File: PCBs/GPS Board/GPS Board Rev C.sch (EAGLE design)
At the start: 4 parts

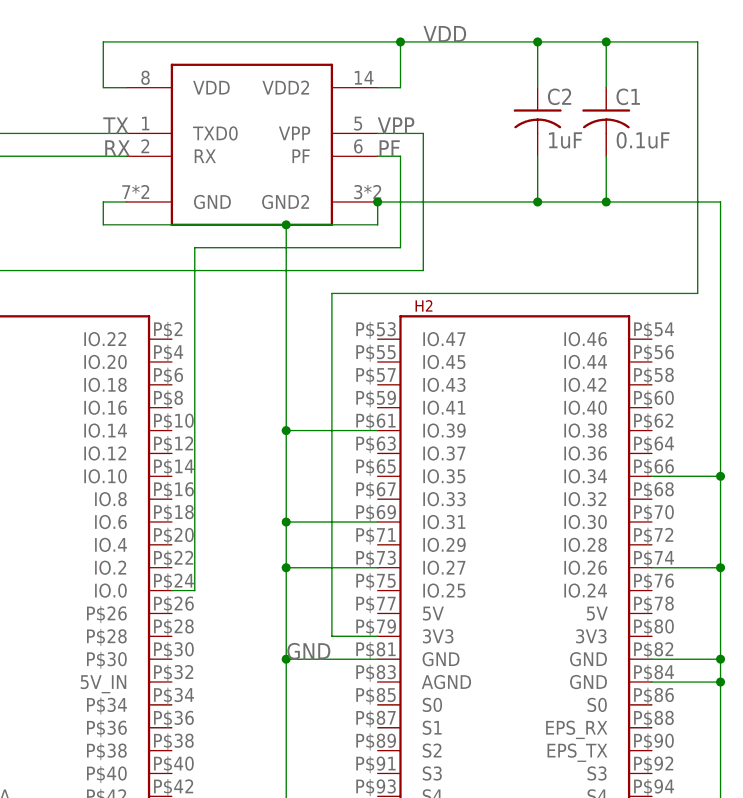
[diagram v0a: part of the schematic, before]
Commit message: Changed GPS power source to an EPS PDM, tweaked trace width
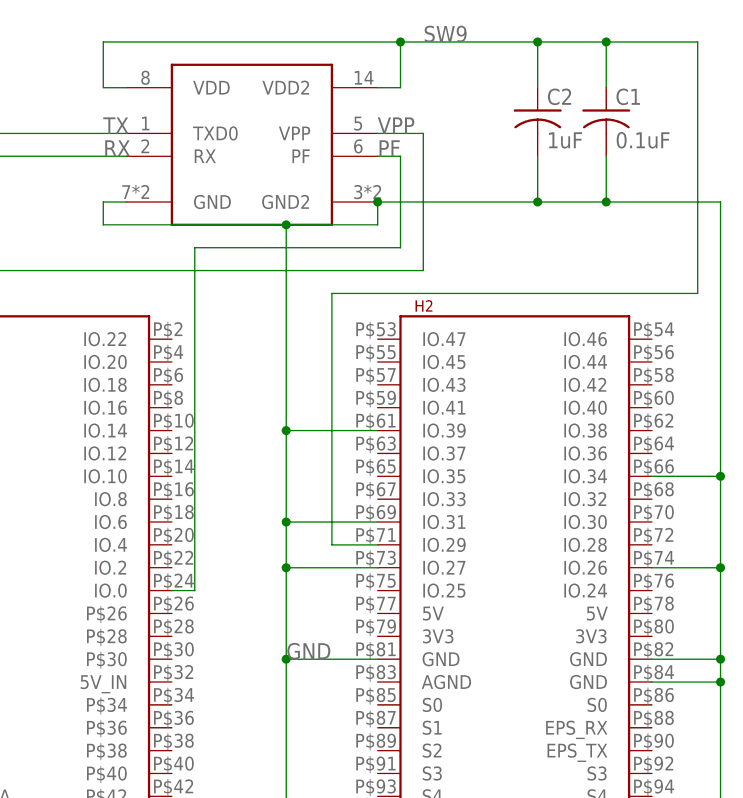
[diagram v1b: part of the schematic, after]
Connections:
- removed net VDD: C1.1, C2.1, U$1.VDD, U$1.VDD2, U$2.3V3@1
- new net SW9: C1.1, C2.1, U$1.VDD, U$1.VDD2, U$2.IO.29
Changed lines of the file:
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@@
 </busses>
 <nets>
-<net name="VDD" class="0">
+<net name="SW9" class="0">
 <segment>
 <wire x1="48.26" y1="91.44" x2="48.26" y2="86.36" width="0.1524" layer="91"/>
@@
 <wire x1="71.12" y1="91.44" x2="81.28" y2="91.44" width="0.1524" layer="91"/>
 <wire x1="81.28" y1="91.44" x2="81.28" y2="63.5" width="0.1524" layer="91"/>
-<wire x1="81.28" y1="63.5" x2="40.64" y2="63.5" width="0.1524" layer="91"/>
-<wire x1="40.64" y1="63.5" x2="40.64" y2="25.4" width="0.1524" layer="91"/>
-<pinref part="U$2" gate="G$1" pin="3V3@1"/>
-<wire x1="40.64" y1="25.4" x2="45.72" y2="25.4" width="0.1524" layer="91"/>
 <pinref part="C2" gate="G$1" pin="1"/>
 <wire x1="63.5" y1="86.36" x2="63.5" y2="91.44" width="0.1524" layer="91"/>
@@
 <pinref part="U$1" gate="G$1" pin="VDD"/>
 <wire x1="15.24" y1="86.36" x2="17.78" y2="86.36" width="0.1524" layer="91"/>
+<wire x1="81.28" y1="63.5" x2="40.64" y2="63.5" width="0.1524" layer="91"/>
+<pinref part="U$2" gate="G$1" pin="IO.29"/>
+<wire x1="40.64" y1="63.5" x2="40.64" y2="35.56" width="0.1524" layer="91"/>
+<wire x1="40.64" y1="35.56" x2="45.72" y2="35.56" width="0.1524" layer="91"/>
 </segment>
 </net>

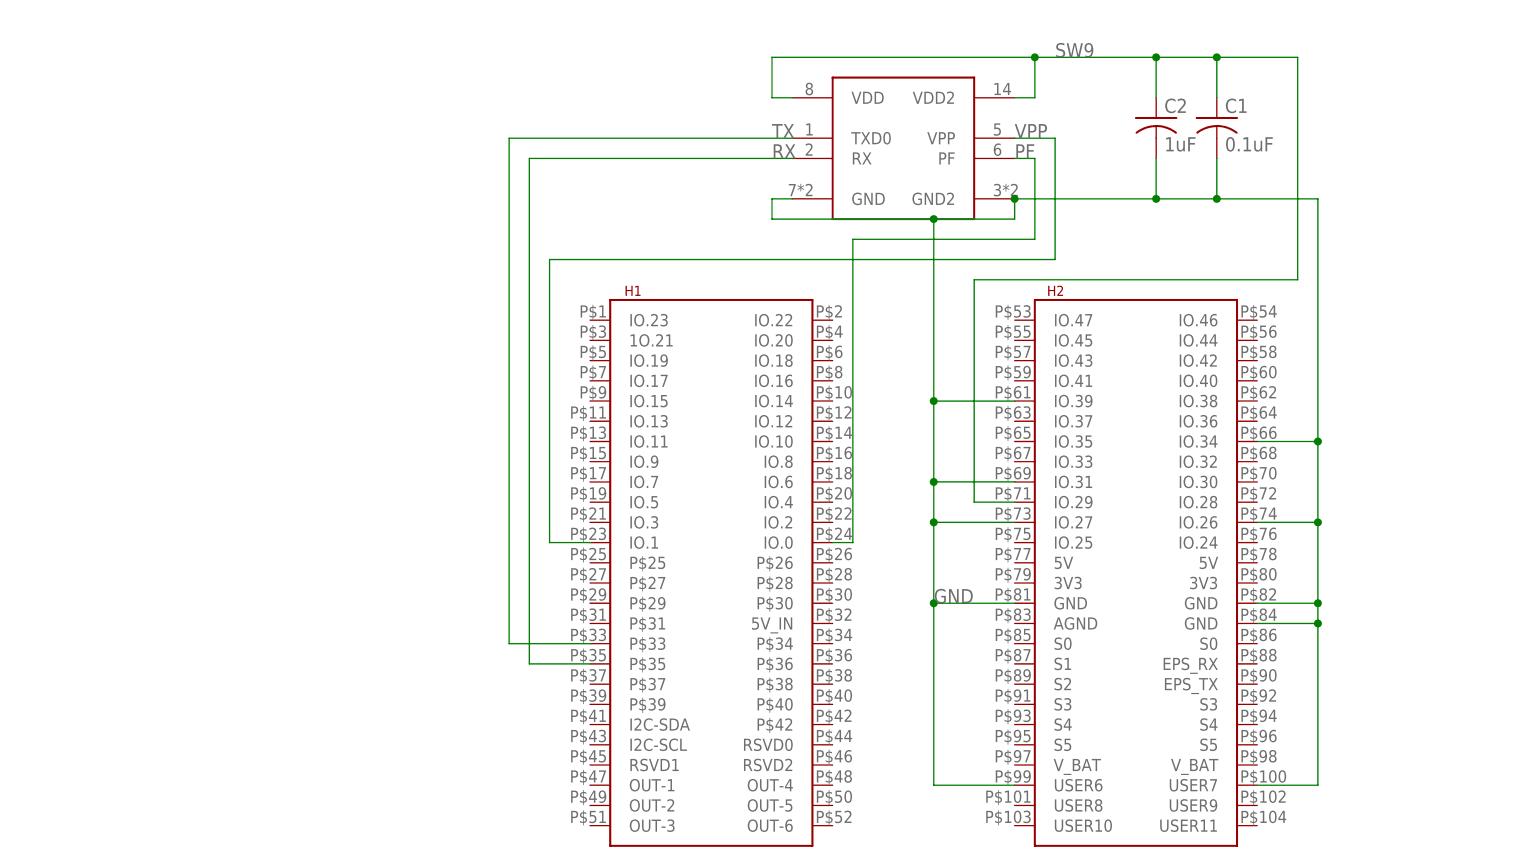
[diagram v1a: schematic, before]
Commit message: Add temp sensors to GPS and Radio boards
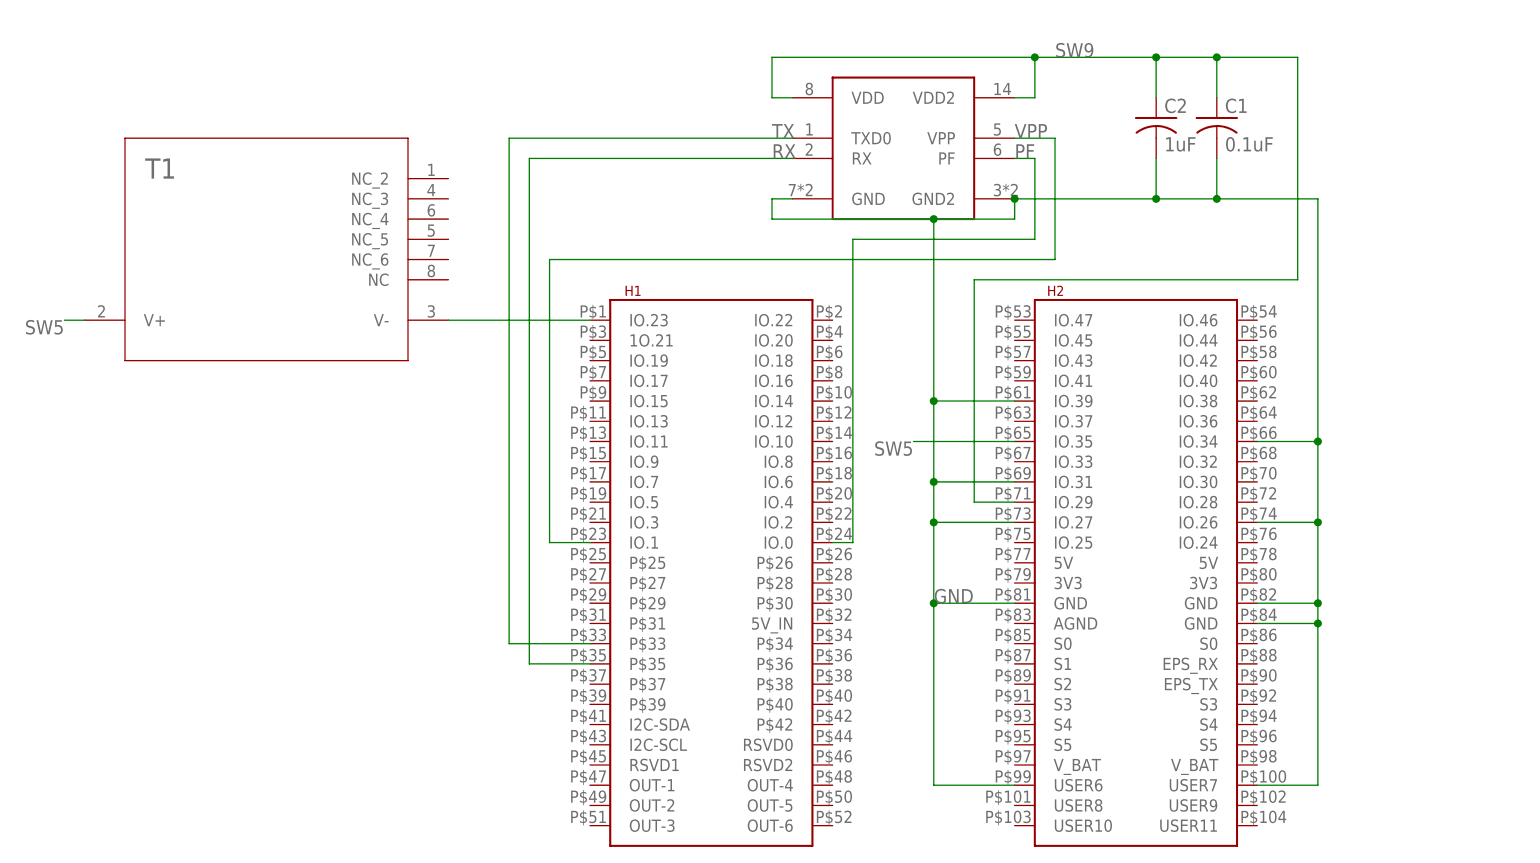
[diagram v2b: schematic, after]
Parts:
- added T1: AD590KRZ, AD590KRZ:AD590KRZ
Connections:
- new net N$1: T1.V-, U$2.IO.23
- new net SW5: T1.V+, U$2.IO.35
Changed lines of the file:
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@@
 <layers>
 <layer number="1" name="Top" color="4" fill="1" visible="no" active="no"/>
+<layer number="2" name="Route2" color="1" fill="3" visible="no" active="no"/>
+<layer number="3" name="Route3" color="4" fill="3" visible="no" active="no"/>
+<layer number="4" name="Route4" color="1" fill="4" visible="no" active="no"/>
+<layer number="5" name="Route5" color="4" fill="4" visible="no" active="no"/>
+<layer number="6" name="Route6" color="1" fill="8" visible="no" active="no"/>
+<layer number="7" name="Route7" color="4" fill="8" visible="no" active="no"/>
+<layer number="8" name="Route8" color="1" fill="2" visible="no" active="no"/>
+<layer number="9" name="Route9" color="4" fill="2" visible="no" active="no"/>
+<layer number="10" name="Route10" color="1" fill="7" visible="no" active="no"/>
+<layer number="11" name="Route11" color="4" fill="7" visible="no" active="no"/>
+<layer number="12" name="Route12" color="1" fill="5" visible="no" active="no"/>
+<layer number="13" name="Route13" color="4" fill="5" visible="no" active="no"/>
+<layer number="14" name="Route14" color="1" fill="6" visible="no" active="no"/>
+<layer number="15" name="Route15" color="4" fill="6" visible="no" active="no"/>
 <layer number="16" name="Bottom" color="1" fill="1" visible="no" active="no"/>
 <layer number="17" name="Pads" color="2" fill="1" visible="no" active="no"/>
@@
 <layer number="56" name="wert" color="7" fill="1" visible="no" active="no"/>
 <layer number="57" name="tCAD" color="7" fill="1" visible="no" active="no"/>
+<layer number="88" name="SimResults" color="9" fill="1" visible="yes" active="yes"/>
+<layer number="89" name="SimProbes" color="9" fill="1" visible="yes" active="yes"/>
 <layer number="90" name="Modules" color="5" fill="1" visible="yes" active="yes"/>
 <layer number="91" name="Nets" color="2" fill="1" visible="yes" active="yes"/>
@@
 <part name="C2" library="resistor" library_urn="urn:adsk.eagle:library:348" deviceset="C-US" device="C0603" package3d_urn="urn:adsk.eagle:package:26138/1" value="1uF"/>
 <part name="C1" library="resistor" library_urn="urn:adsk.eagle:library:348" deviceset="C-US" device="C0603" package3d_urn="urn:adsk.eagle:package:26138/1" value="0.1uF"/>
+<part name="T1" library="AD590KRZ" deviceset="AD590KRZ" device=""/>
 </parts>
 <sheets>
@@
 <instance part="C2" gate="G$1" x="63.5" y="83.82"/>
 <instance part="C1" gate="G$1" x="71.12" y="83.82"/>
+<instance part="T1" gate="A" x="-66.04" y="53.34"/>
 </instances>
 <busses>
@@
 </segment>
 </net>
+<net name="SW5" class="0">
+<segment>
+<pinref part="U$2" gate="G$1" pin="IO.35"/>
+<wire x1="45.72" y1="43.18" x2="33.02" y2="43.18" width="0.1524" layer="91"/>
+<label x="33.02" y="43.18" size="1.778" layer="95" rot="R180"/>
+</segment>
+<segment>
+<pinref part="T1" gate="A" pin="V+"/>
+<wire x1="-71.12" y1="58.42" x2="-73.66" y2="58.42" width="0.1524" layer="91"/>
+<label x="-73.66" y="58.42" size="1.778" layer="95" rot="R180"/>
+</segment>
+</net>
+<net name="N$1" class="0">
+<segment>
+<pinref part="T1" gate="A" pin="V-"/>
+<pinref part="U$2" gate="G$1" pin="IO.23"/>
+<wire x1="-25.4" y1="58.42" x2="-7.62" y2="58.42" width="0.1524" layer="91"/>
+</segment>
+</net>

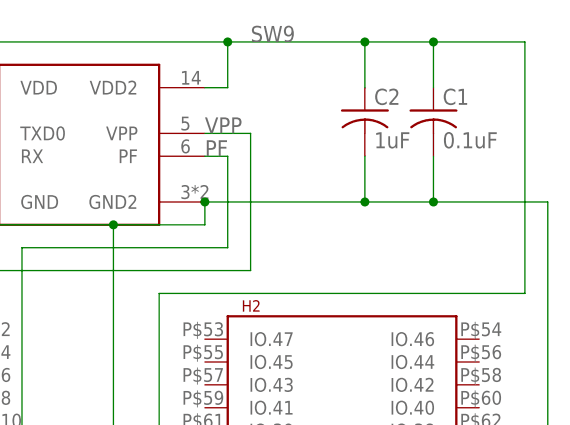
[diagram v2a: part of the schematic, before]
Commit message: Rotated GPS, bumped cap to 10uF
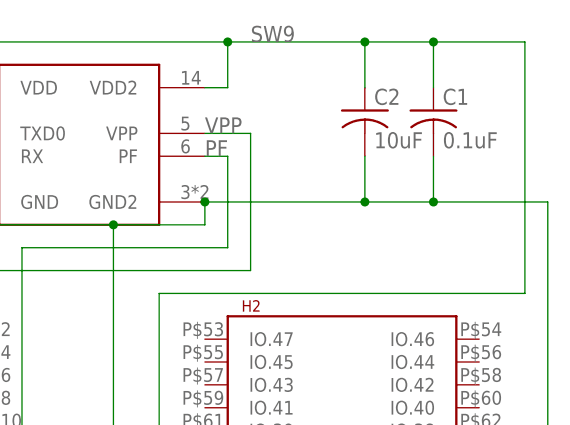
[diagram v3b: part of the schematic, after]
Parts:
- C2: value 1uF -> 10uF
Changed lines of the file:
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@@
 <?xml version="1.0" encoding="utf-8"?>
 <!DOCTYPE eagle SYSTEM "eagle.dtd">
-<eagle version="9.0.1">
+<eagle version="9.1.0">
 <drawing>
 <settings>
@@
 <part name="U$1" library="pinavl1" deviceset="PINAVL1" device=""/>
 <part name="U$2" library="Cubesat" deviceset="PC104" device=""/>
-<part name="C2" library="resistor" library_urn="urn:adsk.eagle:library:348" deviceset="C-US" device="C0603" package3d_urn="urn:adsk.eagle:package:26138/1" value="1uF"/>
+<part name="C2" library="resistor" library_urn="urn:adsk.eagle:library:348" deviceset="C-US" device="C0603" package3d_urn="urn:adsk.eagle:package:26138/1" value="10uF"/>
 <part name="C1" library="resistor" library_urn="urn:adsk.eagle:library:348" deviceset="C-US" device="C0603" package3d_urn="urn:adsk.eagle:package:26138/1" value="0.1uF"/>
 <part name="T1" library="AD590KRZ" deviceset="AD590KRZ" device=""/>

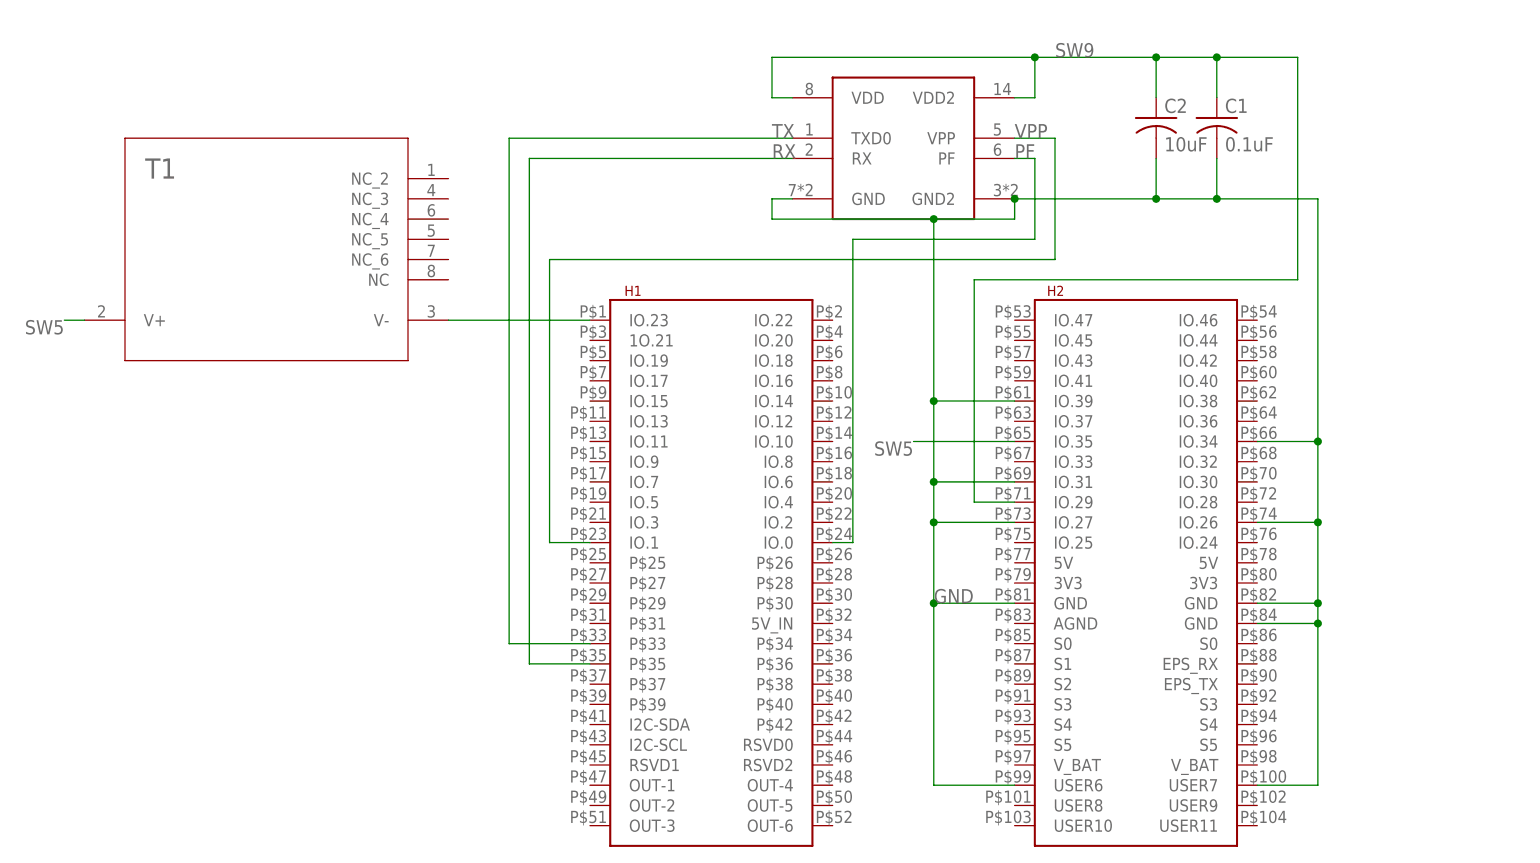
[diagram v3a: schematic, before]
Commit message: Remove temp sensors, tweak trace width
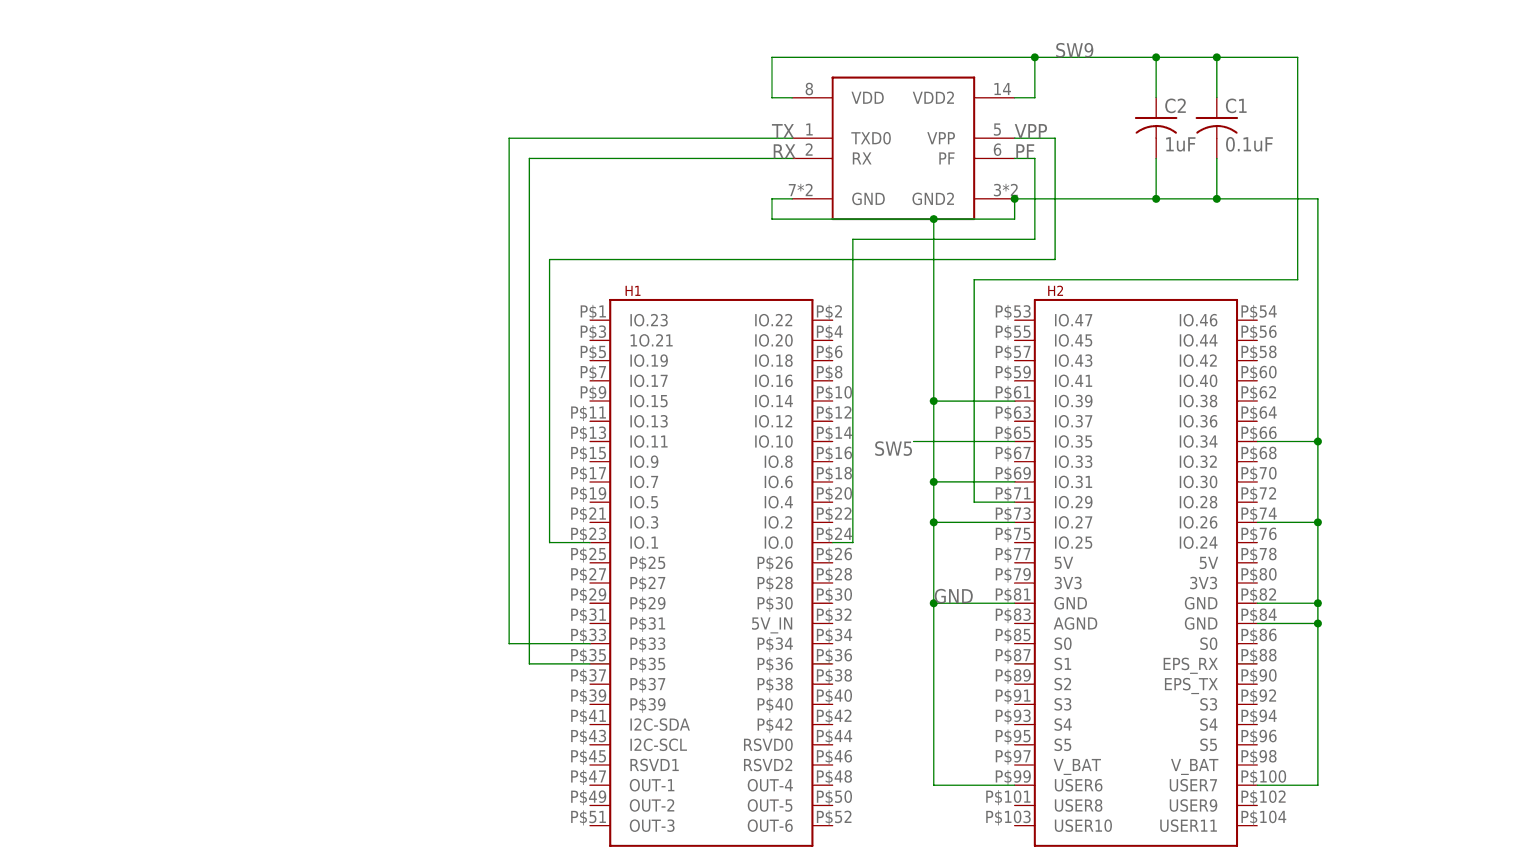
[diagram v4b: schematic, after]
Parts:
- removed T1: AD590KRZ, AD590KRZ:AD590KRZ
- C2: value 10uF -> 1uF
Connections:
- removed net N$1: T1.V-, U$2.IO.23
- net SW5: no longer T1.V+
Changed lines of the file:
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@@
 <part name="U$1" library="pinavl1" deviceset="PINAVL1" device=""/>
 <part name="U$2" library="Cubesat" deviceset="PC104" device=""/>
-<part name="C2" library="resistor" library_urn="urn:adsk.eagle:library:348" deviceset="C-US" device="C0603" package3d_urn="urn:adsk.eagle:package:26138/1" value="10uF"/>
+<part name="C2" library="resistor" library_urn="urn:adsk.eagle:library:348" deviceset="C-US" device="C0603" package3d_urn="urn:adsk.eagle:package:26138/1" value="1uF"/>
 <part name="C1" library="resistor" library_urn="urn:adsk.eagle:library:348" deviceset="C-US" device="C0603" package3d_urn="urn:adsk.eagle:package:26138/1" value="0.1uF"/>
-<part name="T1" library="AD590KRZ" deviceset="AD590KRZ" device=""/>
 </parts>
 <sheets>
@@
 <instance part="C2" gate="G$1" x="63.5" y="83.82"/>
 <instance part="C1" gate="G$1" x="71.12" y="83.82"/>
-<instance part="T1" gate="A" x="-66.04" y="53.34"/>
 </instances>
 <busses>
@@
 <label x="33.02" y="43.18" size="1.778" layer="95" rot="R180"/>
 </segment>
-<segment>
-<pinref part="T1" gate="A" pin="V+"/>
-<wire x1="-71.12" y1="58.42" x2="-73.66" y2="58.42" width="0.1524" layer="91"/>
-<label x="-73.66" y="58.42" size="1.778" layer="95" rot="R180"/>
-</segment>
 </net>
-<net name="N$1" class="0">
-<segment>
-<pinref part="T1" gate="A" pin="V-"/>
-<pinref part="U$2" gate="G$1" pin="IO.23"/>
-<wire x1="-25.4" y1="58.42" x2="-7.62" y2="58.42" width="0.1524" layer="91"/>
-</segment>
-</net>
